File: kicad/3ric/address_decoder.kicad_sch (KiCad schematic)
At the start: 45 parts, among them U1 74LS00, U2 74LS32, U3 74LS04, U4 74LS08, U5 74LS32

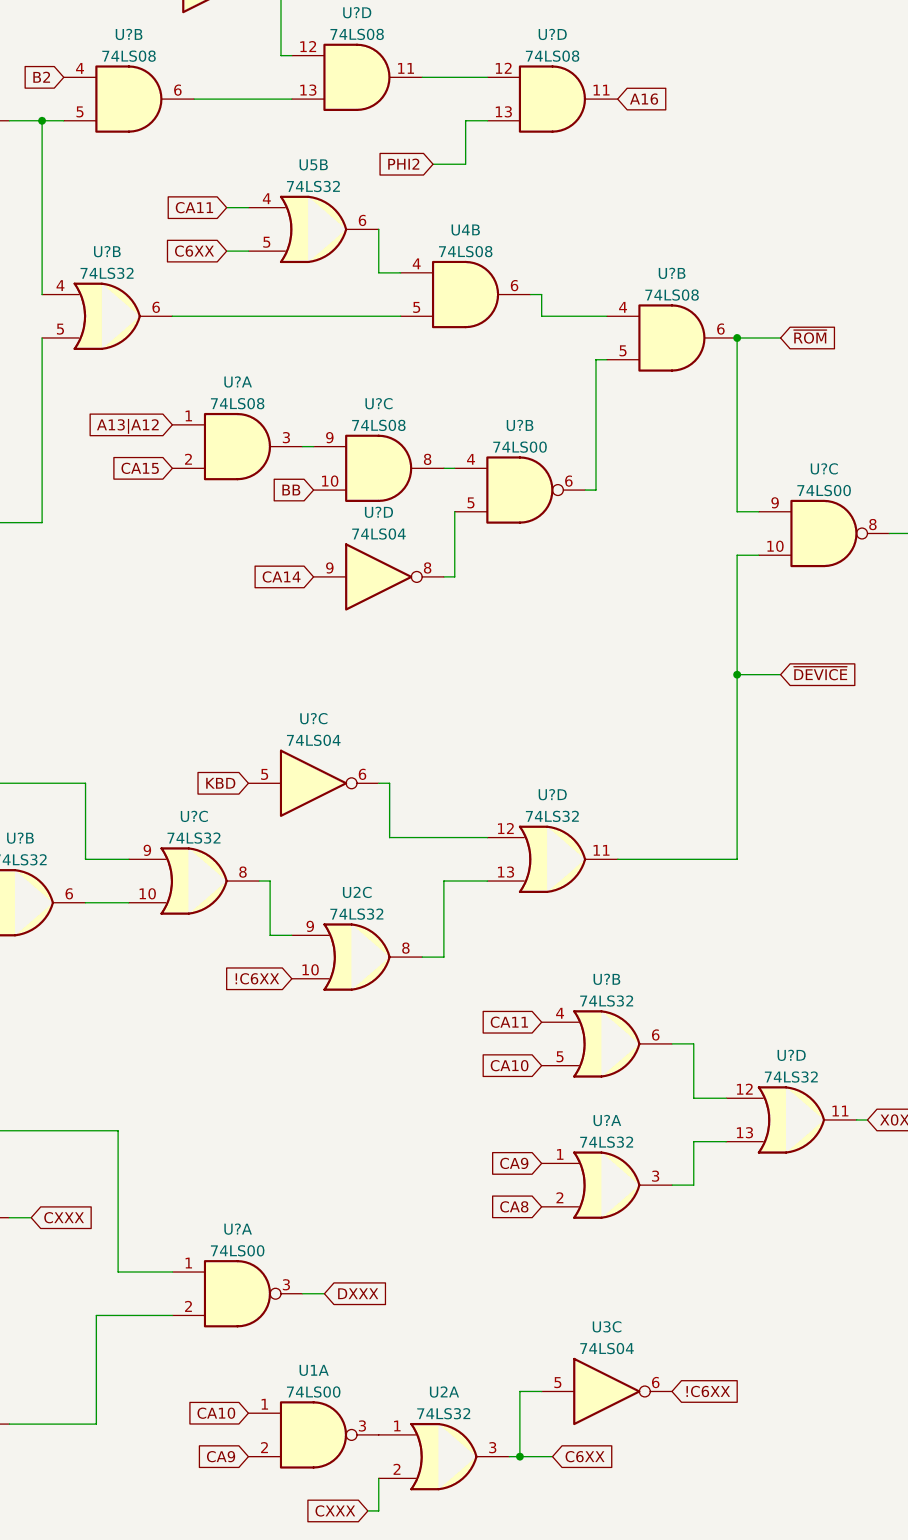
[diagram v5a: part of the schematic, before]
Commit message: update schematic to include disk components
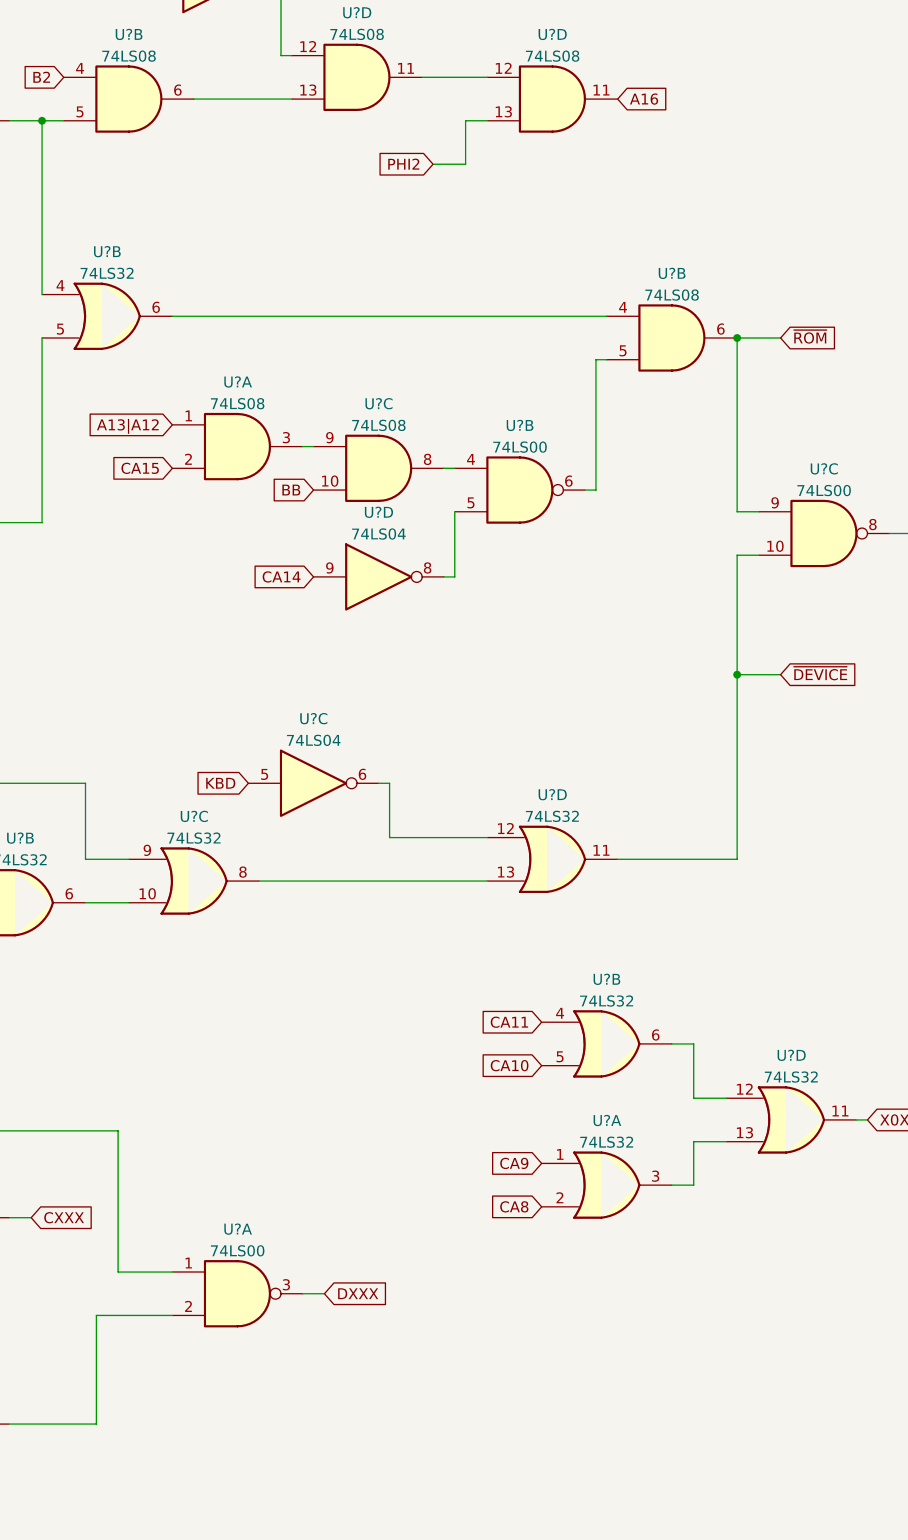
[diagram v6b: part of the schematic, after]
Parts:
- removed U1: 74LS00, symbol 74xx:74LS00
- removed U2, U5: 74LS32, symbol 74xx:74LS32
- removed U3: 74LS04, symbol 74xx:74LS04
- removed U4: 74LS08, symbol 74xx:74LS08
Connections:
- net at U?.13: now also U?.8
- net at U?.6: now also U?.4

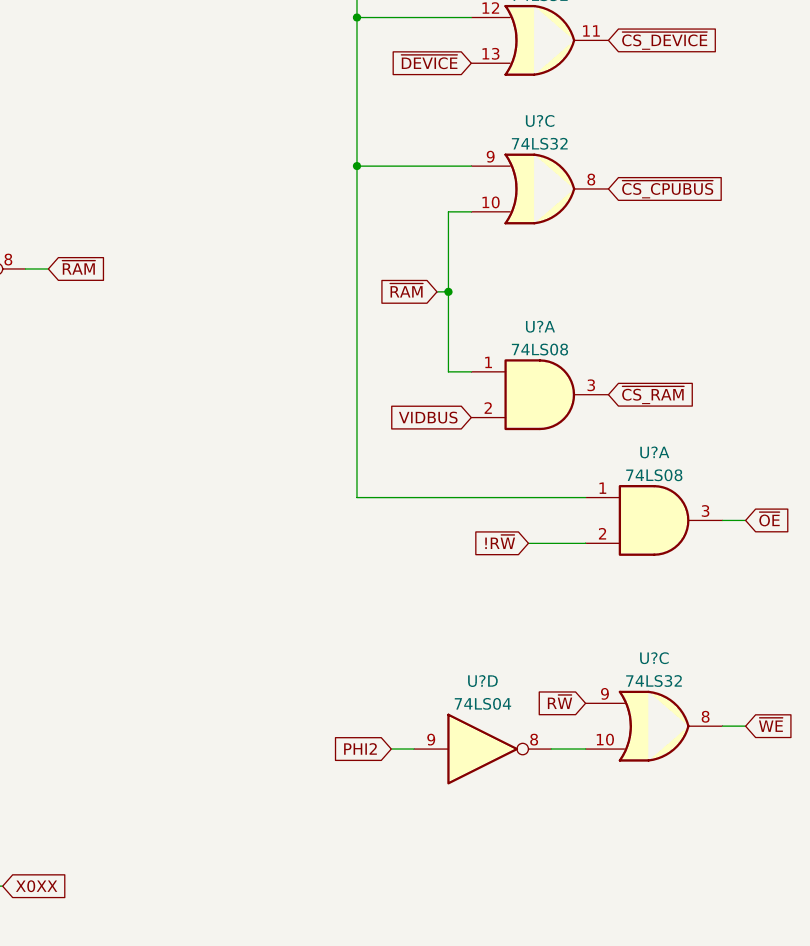
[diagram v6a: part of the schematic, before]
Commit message: update the breadboard map and the schematics
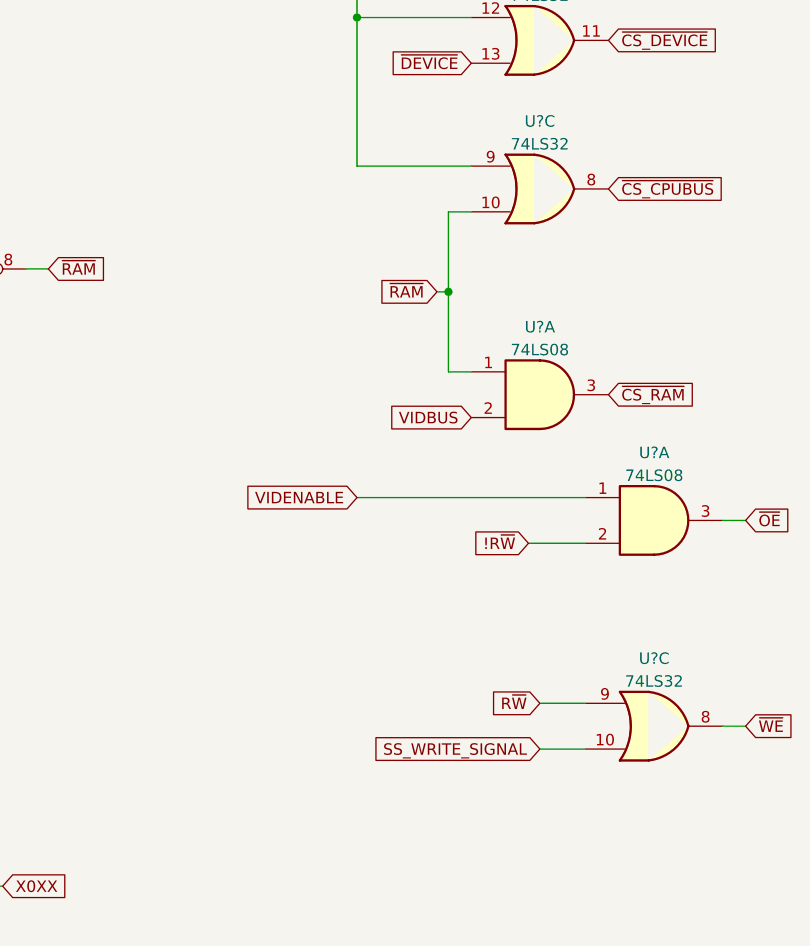
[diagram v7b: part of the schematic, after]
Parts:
- removed U?: 74LS04, symbol 74xx:74LS04
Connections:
- net !VIDENABLE: no longer U?.1
- net SS_WRITE_SIGNAL: now reaches U?.10
- new net VIDENABLE: U?.1
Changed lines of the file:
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@@
 	)
 	(junction
-		(at 229.87 69.85)
-		(diameter 0)
-		(color 0 0 0 0)
-	)
-	(junction
 		(at 229.87 53.34)
 		(diameter 0)
@@
 	(wire
 		(pts
-			(xy 229.87 69.85) (xy 229.87 106.68)
+			(xy 146.05 33.02) (xy 143.51 33.02)
 		)
 		(stroke
@@
 	(wire
 		(pts
-			(xy 146.05 33.02) (xy 143.51 33.02)
+			(xy 46.99 71.12) (xy 46.99 76.2)
 		)
 		(stroke
@@
 	(wire
 		(pts
-			(xy 46.99 71.12) (xy 46.99 76.2)
+			(xy 175.26 97.79) (xy 180.34 97.79)
 		)
 		(stroke
@@
 	(wire
 		(pts
-			(xy 175.26 97.79) (xy 180.34 97.79)
+			(xy 170.18 157.48) (xy 170.18 152.4)
 		)
 		(stroke
@@
 	(wire
 		(pts
-			(xy 170.18 157.48) (xy 170.18 152.4)
+			(xy 143.51 33.02) (xy 143.51 38.1)
 		)
 		(stroke
@@
 	(wire
 		(pts
-			(xy 143.51 33.02) (xy 143.51 38.1)
+			(xy 93.98 33.02) (xy 93.98 53.34)
 		)
 		(stroke
@@
 	(wire
 		(pts
-			(xy 93.98 33.02) (xy 93.98 53.34)
+			(xy 229.87 106.68) (xy 255.27 106.68)
 		)
 		(stroke
@@
 	(wire
 		(pts
-			(xy 229.87 106.68) (xy 255.27 106.68)
+			(xy 250.19 129.54) (xy 255.27 129.54)
 		)
 		(stroke
@@
 	(wire
 		(pts
-			(xy 251.46 134.62) (xy 255.27 134.62)
+			(xy 250.19 134.62) (xy 255.27 134.62)
 		)
 		(stroke
@@
 	(wire
 		(pts
-			(xy 233.68 134.62) (xy 236.22 134.62)
-		)
-		(stroke
-			(width 0)
-			(type default)
-		)
-	)
-	(wire
-		(pts
 			(xy 109.22 55.88) (xy 160.02 55.88)
 		)
@@
 		)
 	)
+	(global_label "R~{W}"
+		(shape input)
+		(at 250.19 129.54 180)
+		(fields_autoplaced yes)
+		(effects
+			(font
+				(size 1.27 1.27)
+			)
+			(justify right)
+		)
+		(property "Intersheetrefs" "${INTERSHEET_REFS}"
+			(at 244.4834 129.54 0)
+			(effects
+				(font
+					(size 1.27 1.27)
+				)
+				(justify right)
+				(hide yes)
+			)
+		)
+	)
 	(global_label "CA15"
 		(shape input)
@@
 		)
 	)
-	(global_label "PHI2"
-		(shape input)
-		(at 233.68 134.62 180)
-		(fields_autoplaced yes)
-		(effects
-			(font
-				(size 1.27 1.27)
-			)
-			(justify right)
-		)
-		(property "Intersheetrefs" "${INTERSHEET_REFS}"
-			(at 226.8521 134.5406 0)
-			(effects
-				(font
-					(size 1.27 1.27)
-				)
-				(justify right)
-				(hide yes)
-			)
-		)
-	)
 	(global_label "~{CS_ROM}"
 		(shape input)
@@
 		)
 	)
-	(global_label "R~{W}"
-		(shape input)
-		(at 255.27 129.54 180)
-		(fields_autoplaced yes)
-		(effects
-			(font
-				(size 1.27 1.27)
-			)
-			(justify right)
-		)
-		(property "Intersheetrefs" "${INTERSHEET_REFS}"
-			(at 250.1355 129.4606 0)
-			(effects
-				(font
-					(size 1.27 1.27)
-				)
-				(justify right)
-				(hide yes)
-			)
-		)
-	)
 	(global_label "!CA12"
 		(shape input)
@@
 		)
 	)
+	(global_label "VIDENABLE"
+		(shape input)
+		(at 229.87 106.68 180)
+		(fields_autoplaced yes)
+		(effects
+			(font
+				(size 1.27 1.27)
+			)
+			(justify right)
+		)
+		(property "Intersheetrefs" "${INTERSHEET_REFS}"
+			(at 216.9062 106.68 0)
+			(effects
+				(font
+					(size 1.27 1.27)
+				)
+				(justify right)
+				(hide yes)
+			)
+		)
+	)
 	(global_label "CA11"
 		(shape input)
@@
 		)
 	)
+	(global_label "SS_WRITE_SIGNAL"
+		(shape input)
+		(at 250.19 134.62 180)
+		(fields_autoplaced yes)
+		(effects
+			(font
+				(size 1.27 1.27)
+			)
+			(justify right)
+		)
+		(property "Intersheetrefs" "${INTERSHEET_REFS}"
+			(at 231.4483 134.5406 0)
+			(effects
+				(font
+					(size 1.27 1.27)
+				)
+				(justify right)
+				(hide yes)
+			)
+		)
+	)
 	(global_label "~{ROM}"
 		(shape input)
@@
 				)
 			)
-		)
-	)
-	(symbol
-		(lib_id "74xx:74LS04")
-		(at 243.84 134.62 0)
-		(unit 4)
-		(exclude_from_sim no)
-		(in_bom yes)
-		(on_board yes)
-		(dnp no)
-		(fields_autoplaced yes)
-		(property "Reference" "U?"
-			(at 243.84 127.1102 0)
-			(effects
-				(font
-					(size 1.27 1.27)
-				)
-			)
-		)
-		(property "Value" "74LS04"
-			(at 243.84 129.6471 0)
-			(effects
-				(font
-					(size 1.27 1.27)
-				)
-			)
-		)
-		(property "Footprint" ""
-			(at 243.84 134.62 0)
-			(effects
-				(font
-					(size 1.27 1.27)
-				)
-				(hide yes)
-			)
-		)
-		(property "Datasheet" "http://www.ti.com/lit/gpn/sn74LS04"
-			(at 243.84 134.62 0)
-			(effects
-				(font
-					(size 1.27 1.27)
-				)
-				(hide yes)
-			)
-		)
-		(property "Description" ""
-			(at 243.84 134.62 0)
-			(effects
-				(font
-					(size 1.27 1.27)
-				)
-				(hide yes)
-			)
-		)
-		(pin "1"
-		)
-		(pin "2"
-		)
-		(pin "3"
-		)
-		(pin "4"
-		)
-		(pin "5"
-		)
-		(pin "6"
-		)
-		(pin "8"
-		)
-		(pin "9"
-		)
-		(pin "10"
-		)
-		(pin "11"
-		)
-		(pin "12"
-		)
-		(pin "13"
-		)
-		(pin "14"
-		)
-		(pin "7"
-		)
-		(instances
-			(project "3ric"
-				(path "/e63e39d7-6ac0-4ffd-8aa3-1841a4541b55/b718fcb1-8742-4b46-85e8-c35e05bc00ea"
-					(reference "U?")
-					(unit 4)
-				)
-			)

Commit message: wiring continued
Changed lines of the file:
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@@
 	(wire
 		(pts
-			(xy 250.19 129.54) (xy 255.27 129.54)
+			(xy 252.73 129.54) (xy 255.27 129.54)
 		)
 		(stroke
@@
 	(wire
 		(pts
-			(xy 250.19 134.62) (xy 255.27 134.62)
+			(xy 252.73 134.62) (xy 255.27 134.62)
 		)
 		(stroke
@@
 	(global_label "R~{W}"
 		(shape input)
-		(at 250.19 129.54 180)
-		(fields_autoplaced yes)
-		(effects
-			(font
-				(size 1.27 1.27)
-			)
-			(justify right)
-		)
-		(property "Intersheetrefs" "${INTERSHEET_REFS}"
-			(at 244.4834 129.54 0)
+		(at 252.73 129.54 180)
+		(fields_autoplaced yes)
+		(effects
+			(font
+				(size 1.27 1.27)
+			)
+			(justify right)
+		)
+		(property "Intersheetrefs" "${INTERSHEET_REFS}"
+			(at 247.0234 129.54 0)
 			(effects
 				(font
@@
 	(global_label "SS_WRITE_SIGNAL"
 		(shape input)
-		(at 250.19 134.62 180)
-		(fields_autoplaced yes)
-		(effects
-			(font
-				(size 1.27 1.27)
-			)
-			(justify right)
-		)
-		(property "Intersheetrefs" "${INTERSHEET_REFS}"
-			(at 231.4483 134.5406 0)
-			(effects
-				(font
+		(at 252.73 134.62 180)
+		(fields_autoplaced yes)
+		(effects
+			(font
+				(size 1.27 1.27)
+			)
+			(justify right)
+		)
+		(property "Intersheetrefs" "${INTERSHEET_REFS}"
+			(at 233.9883 134.5406 0)
+			(effects
+				(font
